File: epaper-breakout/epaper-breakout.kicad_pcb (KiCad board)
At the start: 2 copper layers, 99.6 x 31.2 mm, 60 parts, among them J1 XF2M-3315-1A, J2 C10418, J3 Conn_02x05_Counter_Clockwise, J4 ED060SC4, Q1 IRLML6402, U1 LT1086-3.3, U2 LT1945, U3 L7915, U4 L7815, U5 ESP32-WROVER, U6 CH330N, U7 LM358, U8 74HC4094-normal, U9 MCP9700AT-ETT

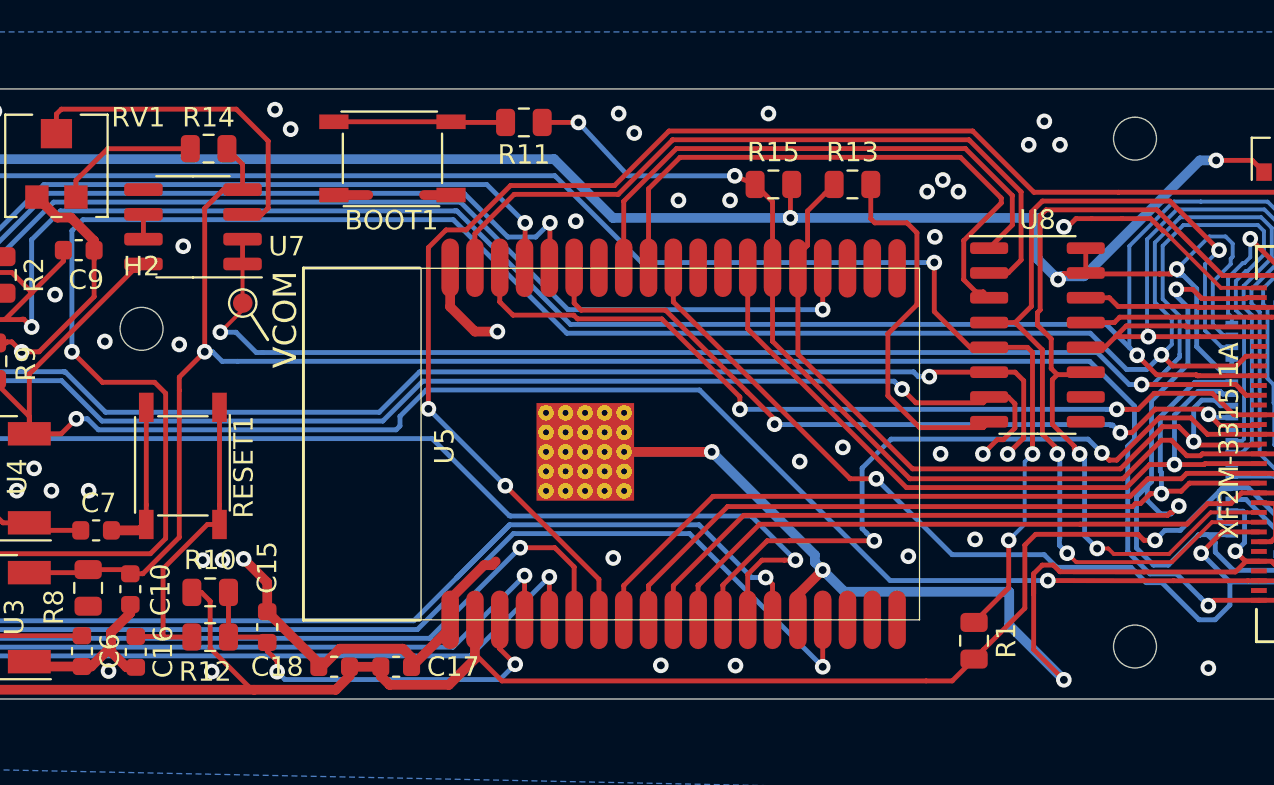
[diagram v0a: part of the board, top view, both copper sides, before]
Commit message: adjust relative position of mounting holes
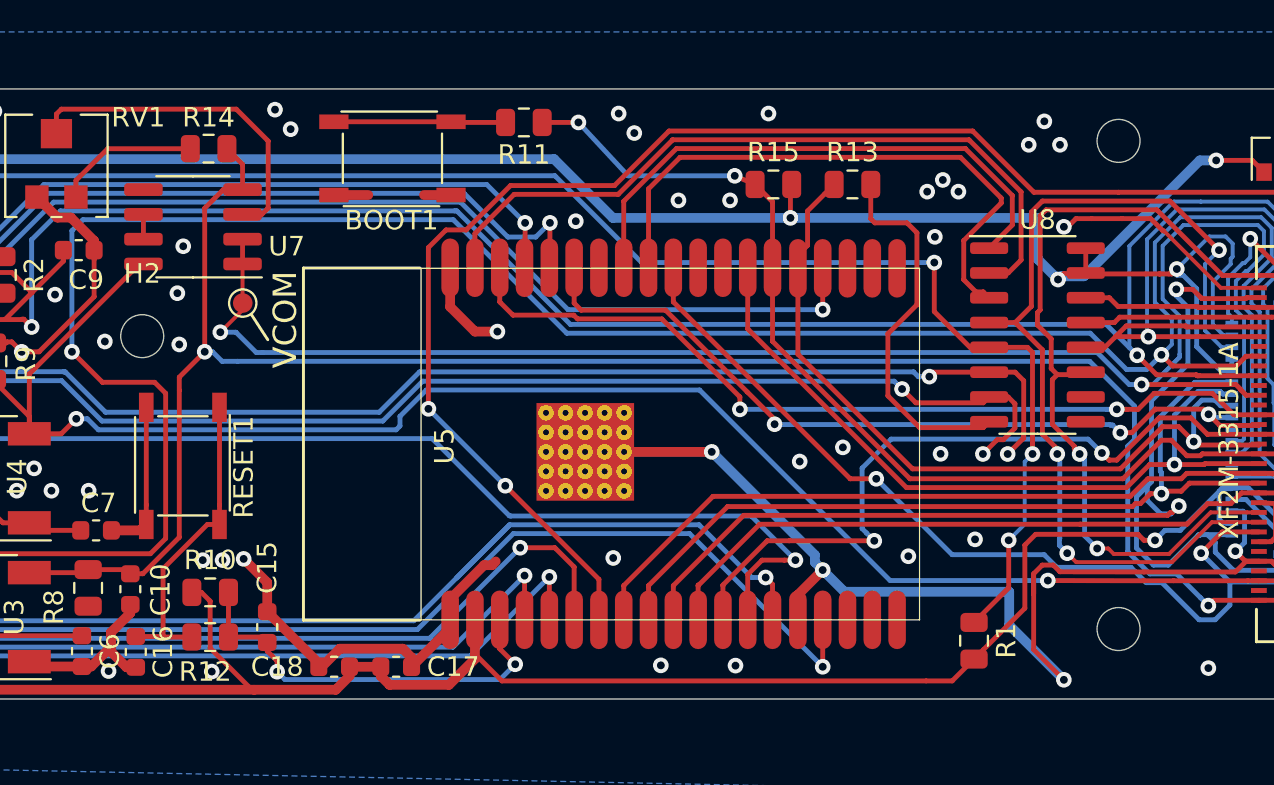
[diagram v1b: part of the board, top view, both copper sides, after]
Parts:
- moved H3 1.23 mm to (111.4, 47.2)
- moved H1 0.85 mm to (111.4, 22.2)
- moved H2 0.38 mm to (61.4, 32.2)
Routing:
- net GND: vias 90 -> 91

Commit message: Fixed value R14 to 390k as 400k doesnt exist and it will work anyway
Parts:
- R14: value 400k -> 390k

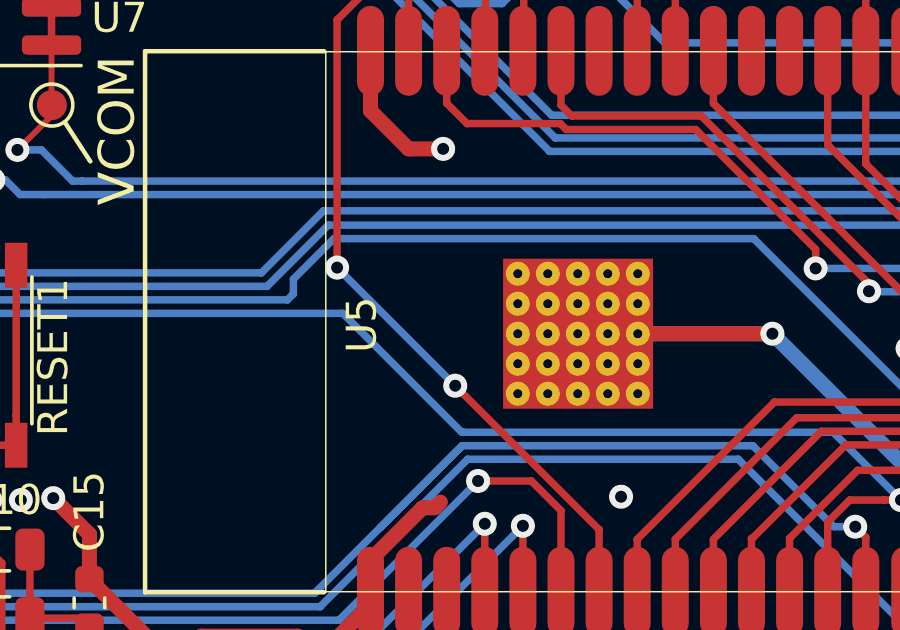
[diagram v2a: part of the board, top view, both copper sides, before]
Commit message: added label with pin numbers for pinheader
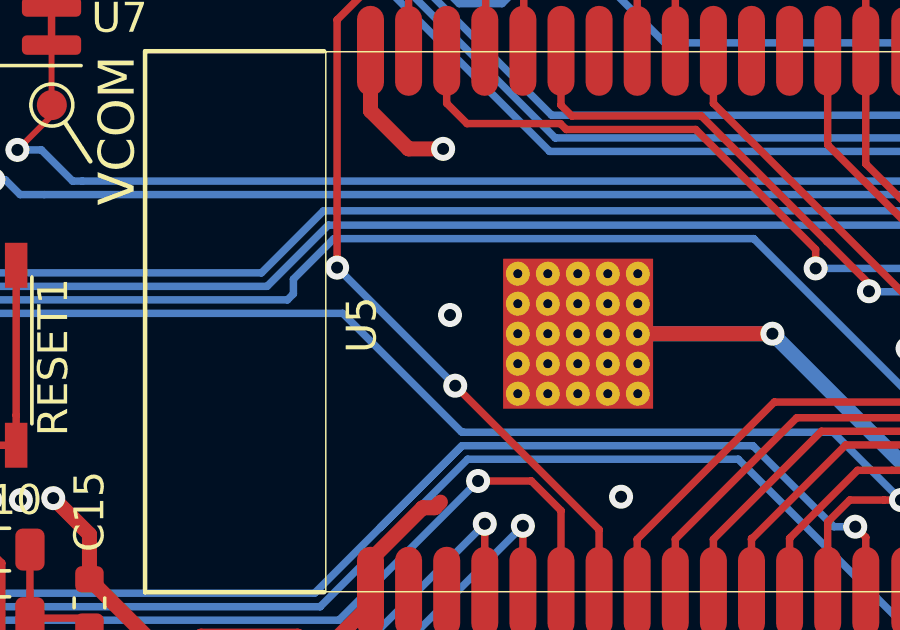
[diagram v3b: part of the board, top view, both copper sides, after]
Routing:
- net GND: vias 91 -> 92
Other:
- board text added: "14, 12 15, 13 GND, 3.3v 34, 5v 36, 39"

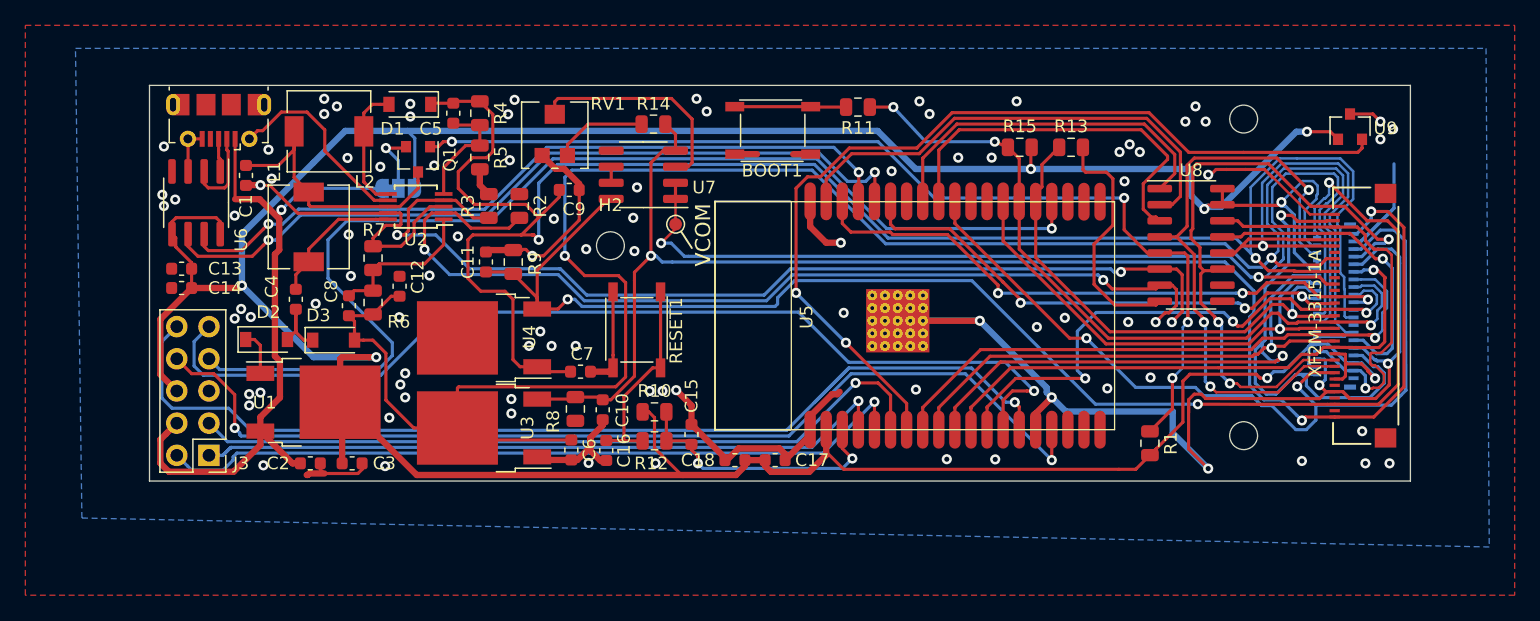
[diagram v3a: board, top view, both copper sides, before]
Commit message: add preliminary 3rd hardware revision
*This is currently untested!*
A new revision of the hardware, reducing power consumption.
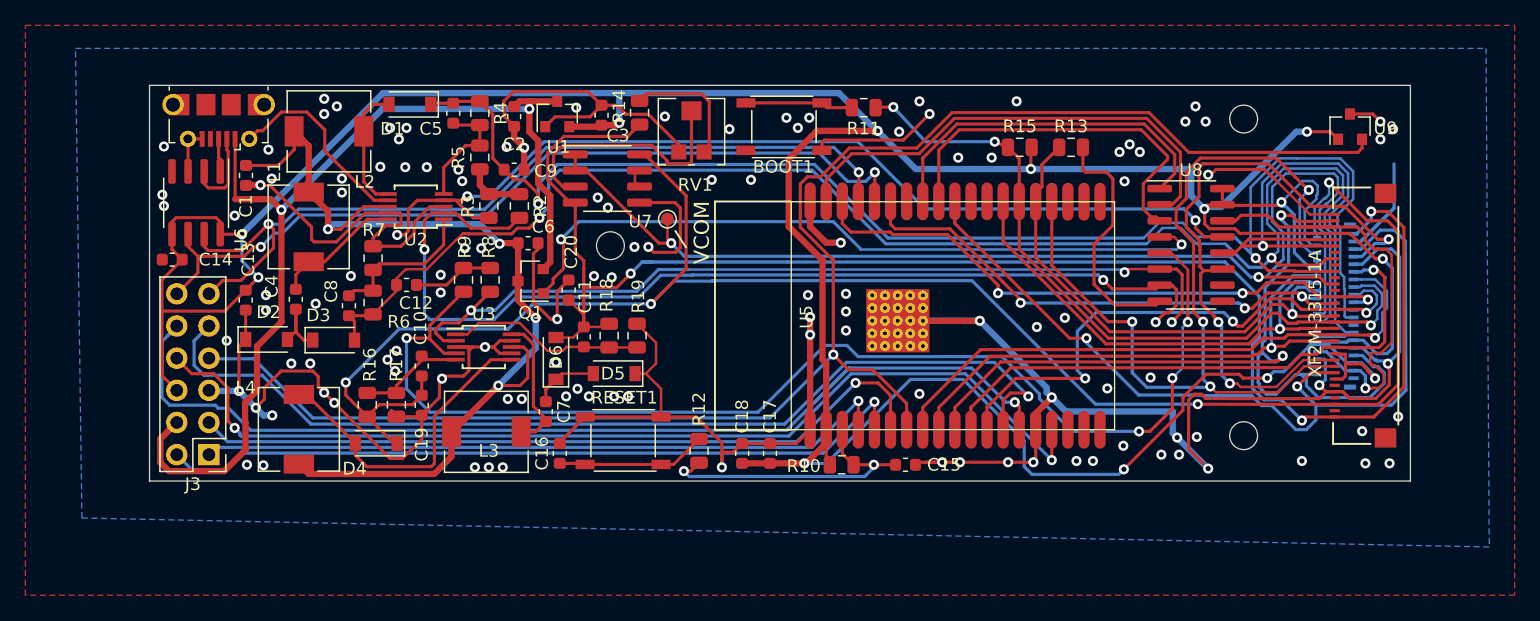
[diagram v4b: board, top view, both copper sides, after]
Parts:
- removed JP1: 5v or 3v to LT1945, Jumper:SolderJumper-3_P1.3mm_Bridged12_RoundedPad1.0x1.5mm
- removed R1: 10k, Resistor_SMD:R_0805_2012Metric
- removed U4: L7815, Package_TO_SOT_SMD:TO-252-2
- added C19: 1uF, Capacitor_SMD:C_0603_1608Metric, F.Cu at (46.5, 44.8)
- added C20: 1uF, Capacitor_SMD:C_0603_1608Metric, F.Cu at (58.1, 35.7)
- added D4: MBR0540, Diode_SMD:D_SOD-123, F.Cu at (42.9, 47.8)
- added D5: MBR0540, Diode_SMD:D_SOD-123, F.Cu at (61.7, 42.3)
- added D6: MBR0540, Diode_SMD:D_SOD-123, F.Cu at (57.1, 41.1)
- added L3: 22uH, Inductor_SMD:L_6.3x6.3_H3, F.Cu at (51.6, 46.9)
- added L4: 22uH, Inductor_SMD:L_6.3x6.3_H3, F.Cu at (36.8, 46.7)
- added R16: 300k, Resistor_SMD:R_0805_2012Metric, F.Cu at (42.2, 44.8)
- added R17: 27k, Resistor_SMD:R_0805_2012Metric, F.Cu at (44.5, 44.8)
- added R18: 110k, Resistor_SMD:R_0805_2012Metric, F.Cu at (61.3, 39.3)
- added R19: 10k, Resistor_SMD:R_0805_2012Metric, F.Cu at (63.5, 39.3)
- C10: value 1uF -> 4.7pF
- C11: value 1uF -> 100pF
- C6: value 0.33uF -> 4.7uF
- C7: value 0.33uF -> 0.1uF
- J3: value Conn_02x05_Counter_Clockwise -> Conn_02x06_Counter_Clockwise; footprint Connector_PinHeader_2.54mm:PinHeader_2x05_P2.54mm_Vertical -> Connector_PinHeader_2.54mm:PinHeader_2x06_P2.54mm_Vertical
- R8, R9: value 39k -> 10k
- U1: value LT1086-3.3 -> MCP1700-3302E_SOT23; footprint Package_TO_SOT_SMD:TO-252-2 -> Package_TO_SOT_SMD:SOT-23
- U3: value L7915 -> LT1945; footprint Package_TO_SOT_SMD:TO-252-2 -> Package_SO:MSOP-10_3x3mm_P0.5mm
- moved C3 33.8 mm to (60.7, 21.9), turned to 270 degrees
- moved C2 31.8 mm to (53.8, 22.0), turned to 90 degrees
- moved U1 29.8 mm to (57.2, 21.8), turned to 90 degrees
- moved C15 17.1 mm to (84.7, 49.5), turned to 180 degrees
- moved C6 16.7 mm to (54.9, 32.0), turned to 0 degrees
- moved R10 15.4 mm to (79.7, 49.5)
- moved C10 14.7 mm to (46.5, 41.7)
- moved Q1 13.1 mm to (55.1, 35.0), turned to 180 degrees
- moved R8 12.2 mm to (51.9, 34.9)
- moved RV1 10.8 mm to (67.8, 23.2)
- moved C11 9.73 mm to (59.3, 39.4)
- moved RESET1 8.82 mm to (62.4, 47.6), turned to 0 degrees
- moved U3 6.39 mm to (51.4, 40.2), turned to 0 degrees
- moved C13 5.63 mm to (32.6, 36.5), turned to 270 degrees
- moved C9 4.63 mm to (53.8, 26.2)
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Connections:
- net /NEG_CTRL renamed /CTRL-20V
- C1 pad 1: Net-(C1-Pad1) -> EPD_POWER
- C10 pad 1: /-15V -> Net-(C10-Pad1)
- C10 pad 2: GND -> /15V
- C11 pad 1: /15V -> Net-(C11-Pad1)
- C11 pad 2: GND -> /-15V
- C13 pad 1: +3.3V -> /+3.3V
- C14 pad 1: +3.3V -> /+3.3V
- C17 pad 1: +3.3V -> /+3.3V
- C18 pad 2: +3.3V -> /+3.3V
- C3 pad 2: +3.3V -> /+3.3V
- C6 pad 1: /-20V -> EPD_POWER
- C7 pad 1: GND -> Net-(C7-Pad1)
- C7 pad 2: /+22V -> Net-(C7-Pad2)
- J1 pad 11: +3.3V -> /+3.3V
- J1 pad 2: Net-(J1-Pad2) -> (no net)
- J1 pad 21: Net-(J1-Pad21) -> (no net)
- J1 pad 23: Net-(J1-Pad23) -> (no net)
- J1 pad 25: Net-(J1-Pad25) -> (no net)
- J1 pad 27: Net-(J1-Pad27) -> (no net)
- J1 pad 30: /EP_UD -> /+3.3V
- J1 pad 34: Net-(J1-Pad34) -> (no net)
- J1 pad 35: Net-(J1-Pad35) -> (no net)
- J1 pad 4: Net-(J1-Pad4) -> (no net)
- J1 pad 6: Net-(J1-Pad6) -> (no net)
- J1 pad 7: +3.3V -> /+3.3V
- J2 pad 4: Net-(J2-Pad4) -> (no net)
- J3 pad 6: +3.3V -> /+3.3V
- J3 pad 7: /CS0 -> /A1
- J4 pad 10: +3.3V -> /+3.3V
- J4 pad 20: Net-(J4-Pad20) -> (no net)
- J4 pad 21: Net-(J4-Pad21) -> (no net)
- J4 pad 25: Net-(J4-Pad25) -> (no net)
- J4 pad 26: Net-(J4-Pad26) -> (no net)
- J4 pad 29: /EP_UD -> /+3.3V
- J4 pad 30: +3.3V -> /+3.3V
- J4 pad 35: +3.3V -> /+3.3V
- J4 pad 36: +3.3V -> /+3.3V
- J4 pad 39: Net-(J4-Pad39) -> (no net)
- J4 pad 4: +3.3V -> /+3.3V
- J4 pad 8: +3.3V -> /+3.3V
- L1 pad 2: Net-(C1-Pad1) -> EPD_POWER
- L2 pad 2: Net-(C1-Pad1) -> EPD_POWER
- Q1 pad 1: ~SMPS_CTRL -> /~SMPS_CTRL
- Q1 pad 2: Net-(JP1-Pad2) -> 5V
- Q1 pad 3: Net-(C1-Pad1) -> EPD_POWER
- R10 pad 1: +3.3V -> /+3.3V
- R15 pad 2: +3.3V -> /+3.3V
- R3 pad 1: /POS_CTRL -> /CTRL+22V
- R8 pad 1: GND -> /CTRL-15V
- R8 pad 2: /-15V -> GND
- R9 pad 1: /15V -> /CTRL+15V
- U1 pad 2: +3.3V -> /+3.3V
- U2 pad 4: /POS_CTRL -> /CTRL+22V
- U2 pad 8: Net-(C1-Pad1) -> EPD_POWER
- U3 pad 1: GND -> Net-(C11-Pad1)
- U3 pad 2: /-20V -> /CTRL-15V
- U3 pad 3: /-15V -> GND
- U5 pad 17: Net-(U5-Pad17) -> (no net)
- U5 pad 18: Net-(U5-Pad18) -> (no net)
- U5 pad 19: Net-(U5-Pad19) -> (no net)
- U5 pad 2: +3.3V -> /+3.3V
- U5 pad 20: Net-(U5-Pad20) -> (no net)
- U5 pad 21: Net-(U5-Pad21) -> (no net)
- U5 pad 22: Net-(U5-Pad22) -> (no net)
- U5 pad 23: /CS0 -> /EP_LE
- U5 pad 27: Net-(U5-Pad27) -> (no net)
- U5 pad 28: Net-(U5-Pad28) -> (no net)
- U5 pad 32: Net-(U5-Pad32) -> (no net)
- U5 pad 7: /V_TEMP -> /A1
- U6 pad 4: Net-(U6-Pad4) -> (no net)
- U6 pad 5: +3.3V -> /+3.3V
- U6 pad 8: +3.3V -> /+3.3V
- U8 pad 10: Net-(U8-Pad10) -> (no net)
- U8 pad 13: /EP_UD -> /CTRL+22V
- U8 pad 15: +3.3V -> /+3.3V
- U8 pad 16: +3.3V -> /+3.3V
- U8 pad 4: /EP_LE -> /~SMPS_CTRL
- U8 pad 5: ~SMPS_CTRL -> /CTRL+15V
- U8 pad 6: /POS_CTRL -> /CTRL-15V
- U8 pad 9: Net-(U8-Pad9) -> (no net)
- U9 pad 1: +3.3V -> /+3.3V
- U9 pad 2: /V_TEMP -> /A1
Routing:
- net /+3.3V: track 0.00 -> 306.9 mm, vias 0 -> 13
- net +3.3V: track 294.5 -> 0.00 mm, vias 8 -> 0
- net /A1: track 0.00 -> 126.2 mm, vias 0 -> 1
- net GND: track 255.9 -> 368.8 mm, vias 92 -> 122
- net /CTRL+15V: track 0.00 -> 94.8 mm, vias 0 -> 4
- net /CS0: track 90.7 -> 0.00 mm, vias 1 -> 0
- net EPD_POWER: track 0.00 -> 81.7 mm, vias 0 -> 4
- net ~SMPS_CTRL: track 80.3 -> 0.00 mm, vias 4 -> 0
- net /POS_CTRL: track 79.2 -> 0.00 mm, vias 3 -> 0
- net /CTRL+22V: track 0.00 -> 76.8 mm, vias 0 -> 3
- net /V_TEMP: track 72.0 -> 0.00 mm, vias 2 -> 0
- net /CTRL-15V: track 0.00 -> 69.6 mm, vias 0 -> 3
- net /~SMPS_CTRL: track 0.00 -> 57.6 mm, vias 0 -> 2
- net /-20V: track 156.5 -> 117.6 mm
- net /+22V: track 147.2 -> 115.5 mm
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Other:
- board text added: "RX TX 14 12 35 13 G 3.3V 34 5V 36 39"
- board text removed: "14, 12 15, 13 GND, 3.3v 34, 5v 36, 39"

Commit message: update captions
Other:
- board text added: "EPaper Breakout v3 by Valentin Roland 2020"
- board text added: "RX TX 14 12 35/Tmp 13 G 3.3V 34 5V 36 39"
- board text removed: "3v"
- board text removed: "5v"
- board text removed: "Booster VIN"
- board text removed: "EPaper Breakout v2 ED097OC4/ED060SC4 by Valentin Roland 2020"
- board text removed: "RX TX 14 12 35 13 G 3.3V 34 5V 36 39"

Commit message: add 3d models for coils
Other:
- board text added: "RX TX 14 12 35/Tmp 13 GND 3.3V 34 5V 36 39"
- board text removed: "RX TX 14 12 35/Tmp 13 G 3.3V 34 5V 36 39"

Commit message: renamve to v4 to differentiate from improved v2
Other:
- board text added: "EPaper Breakout v4 by Valentin Roland 2020"
- board text removed: "EPaper Breakout v3 by Valentin Roland 2020"
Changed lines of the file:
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@@
   )
   (setup
-    (last_trace_width 0.25)
+    (last_trace_width 0.2)
     (user_trace_width 0.2)
     (user_trace_width 0.5)
@@
     (effects (font (size 1.2 1.2) (thickness 0.2)))
   )
-  (gr_text "EPaper Breakout v3\nby Valentin Roland 2020" (at 93.4 24.4 180) (layer B.SilkS)
+  (gr_text "EPaper Breakout v4\nby Valentin Roland 2020" (at 93.4 24.4 180) (layer B.SilkS)
     (effects (font (size 1 1) (thickness 0.15)) (justify mirror))
   )
